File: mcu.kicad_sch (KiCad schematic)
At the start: 42 parts, among them J2 RJ45_Shielded, J4 Micro_SD_Card_Det1, J6 Conn_01x03_Pin, J7 RFShield_TwoPieces, SW1 SW_Push, SW2 SW_Push, SW3 SW_Push, SW4 SW_Push, U1 nRF54L15-QFXX, U9 TPD6F003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

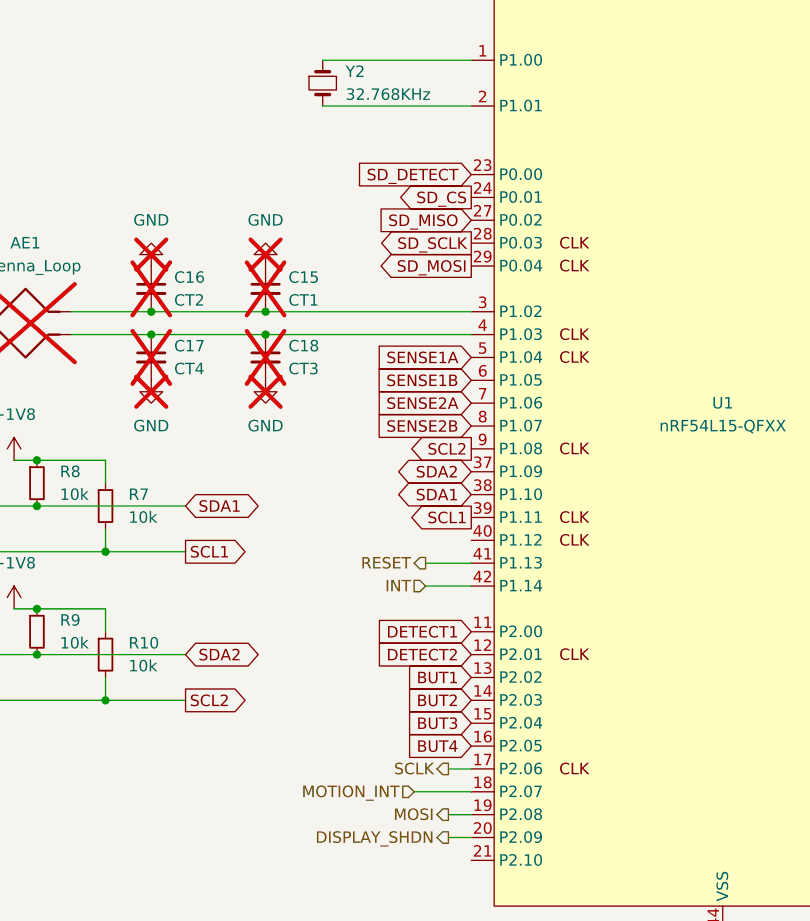
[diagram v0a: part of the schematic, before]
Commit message: start routing MCU + switch out pin assignments
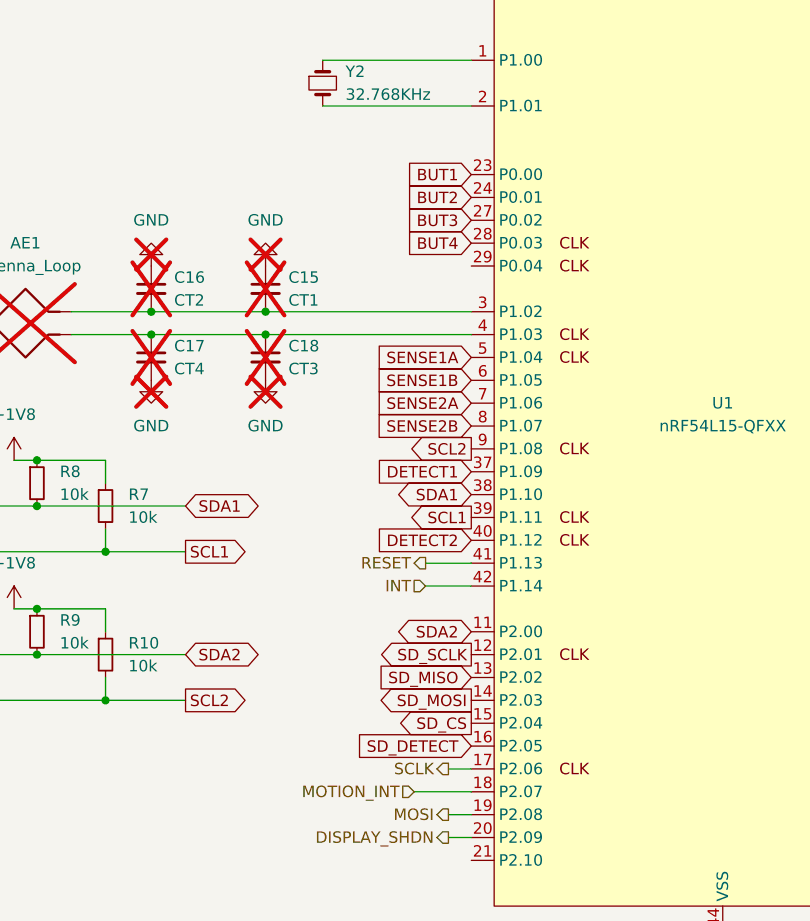
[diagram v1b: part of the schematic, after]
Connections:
- net BUT1: now also U1.23 (P0.00); no longer U1.13 (P2.02)
- net BUT2: now also U1.24 (P0.01); no longer U1.14 (P2.03)
- net BUT3: now also U1.27 (P0.02); no longer U1.15 (P2.04)
- net BUT4: now also U1.28 (P0.03); no longer U1.16 (P2.05)
- net DETECT1: now also U1.37 (P1.09); no longer U1.11 (P2.00)
- net DETECT2: now also U1.40 (P1.12); no longer U1.12 (P2.01)
- net SDA2: now also U1.11 (P2.00); no longer U1.37 (P1.09)
- net SD_CS: now also U1.15 (P2.04); no longer U1.24 (P0.01)
- net SD_DETECT: now also U1.16 (P2.05); no longer U1.23 (P0.00)
- net SD_MISO: now also U1.13 (P2.02); no longer U1.27 (P0.02)
- net SD_MOSI: now also U1.14 (P2.03); no longer U1.29 (P0.04)
- net SD_SCLK: now also U1.12 (P2.01); no longer U1.28 (P0.03)

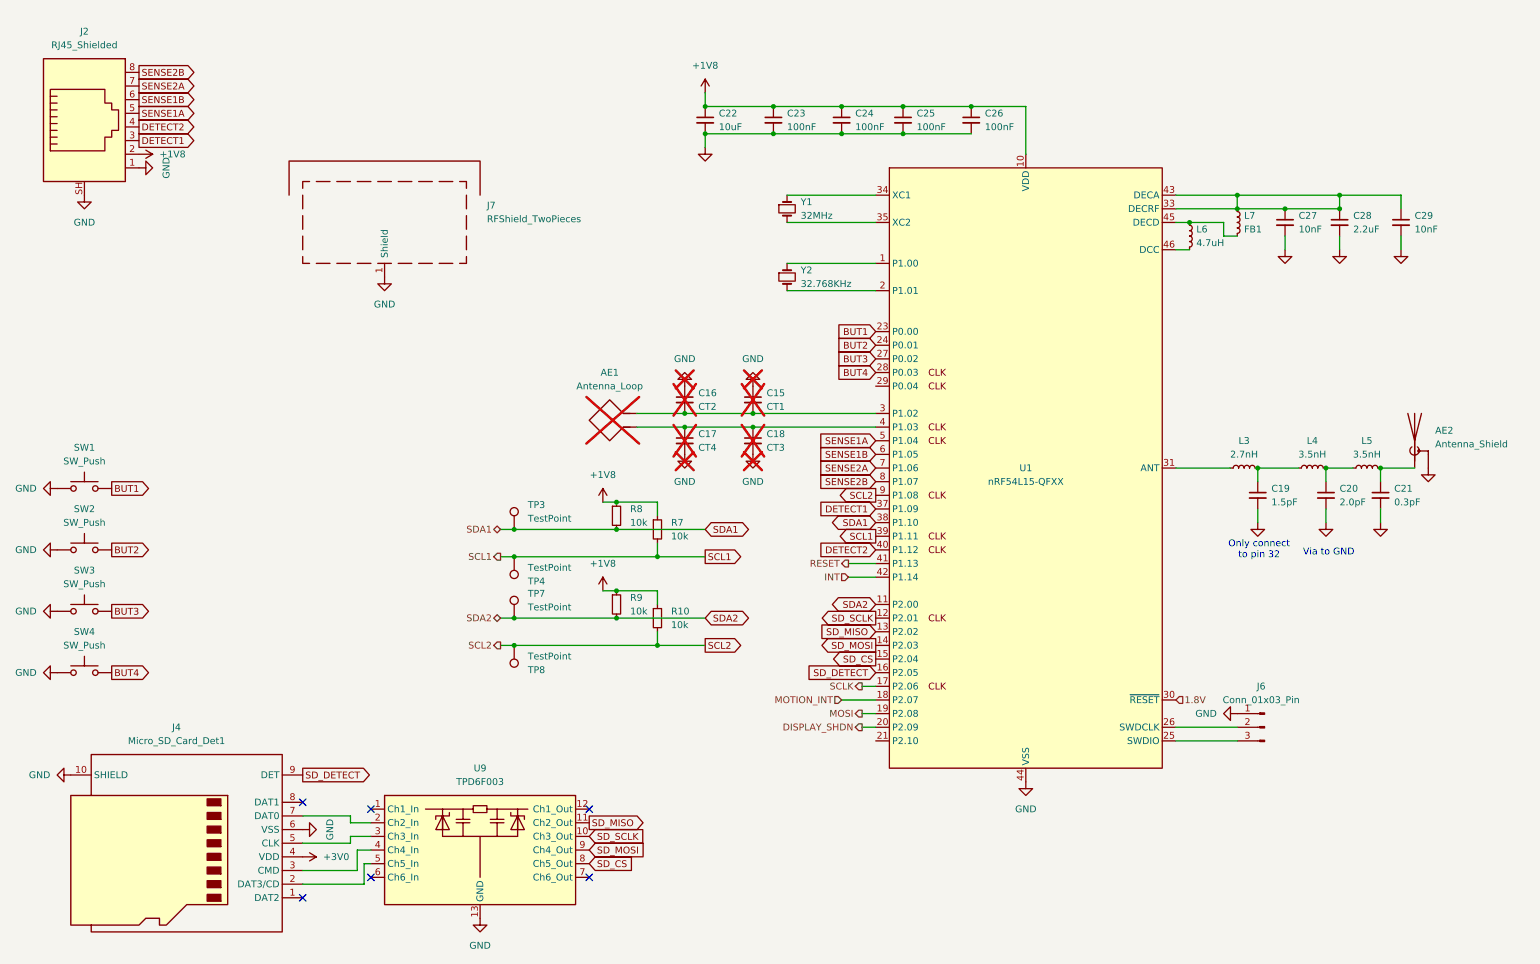
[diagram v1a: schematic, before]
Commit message: replace RJ45 with JST GH connector, add 2 I2C capable GPIOs to output port
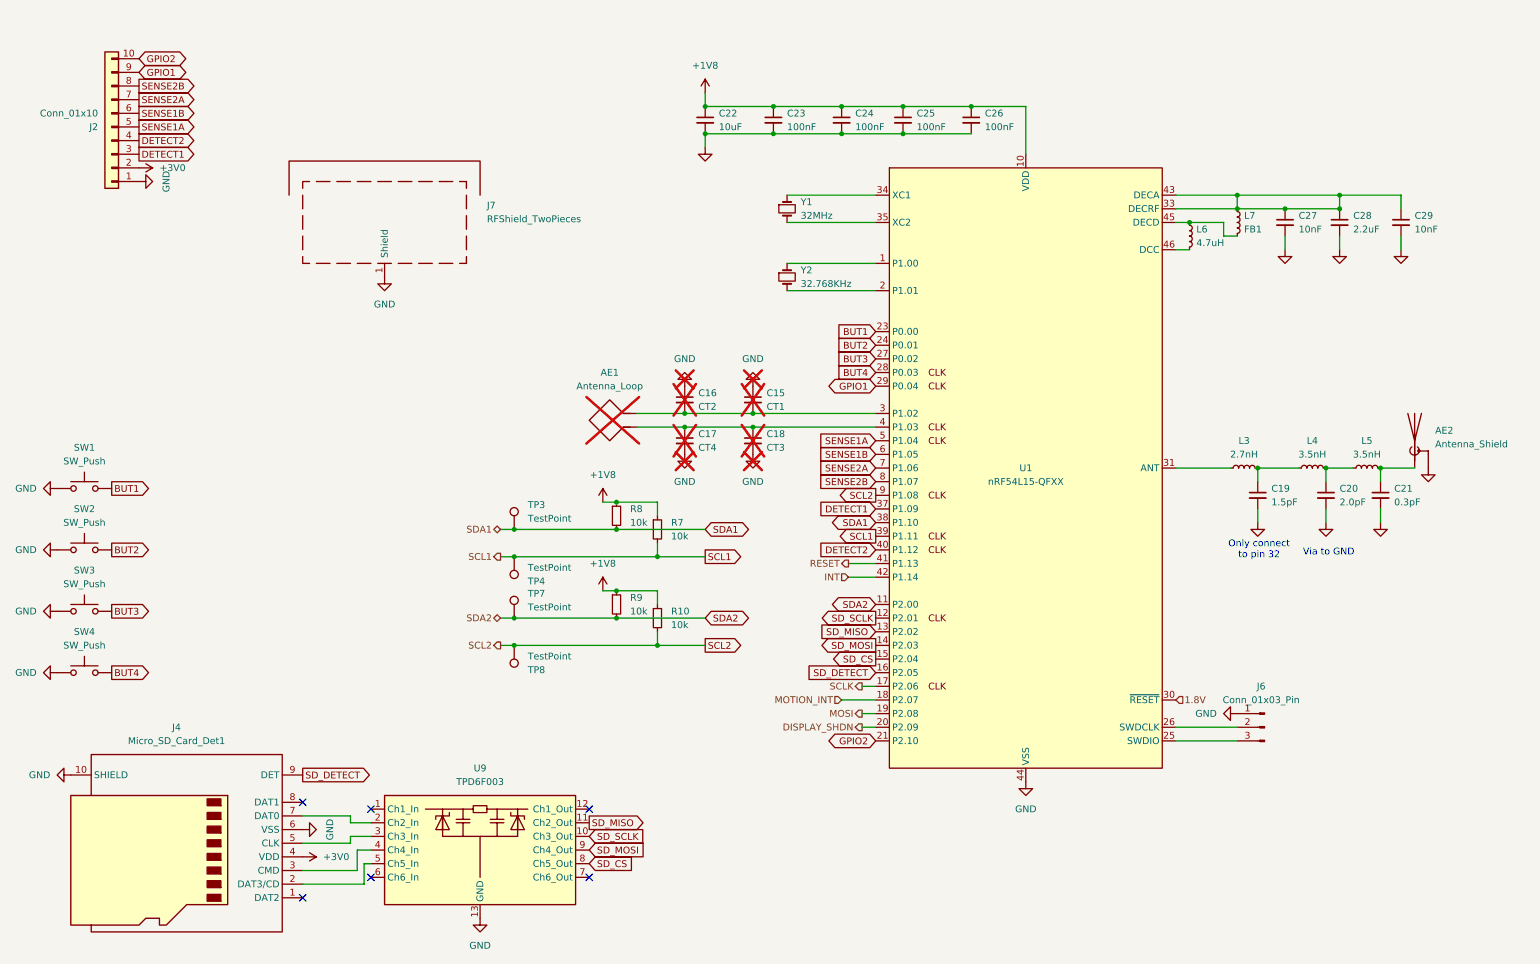
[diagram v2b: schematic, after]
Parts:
- removed J2: RJ45_Shielded, Connector_RJ:RJ45_Amphenol_RJHSE538X, symbol Connector:RJ45_Shielded
- added J2: Conn_01x10, Connector_JST:JST_GH_SM10B-GHS-TB_1x10-1MP_P1.25mm_Horizontal, symbol Connector_Generic:Conn_01x10
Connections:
- net +3V0: now also J2.2 (Pin_2)
- net DETECT1: now also J2.3 (Pin_3)
- net DETECT2: now also J2.4 (Pin_4)
- net GND: now also J2.1 (Pin_1)
- net SENSE1A: now also J2.5 (Pin_5)
- net SENSE1B: now also J2.6 (Pin_6)
- net SENSE2A: now also J2.7 (Pin_7)
- net SENSE2B: now also J2.8 (Pin_8)
- net GPIO2: now reaches U1.21 (P2.10)
- net GPIO2: now also J2.10 (Pin_10)
- net GPIO1: now reaches U1.29 (P0.04)
- net GPIO1: now also J2.9 (Pin_9)

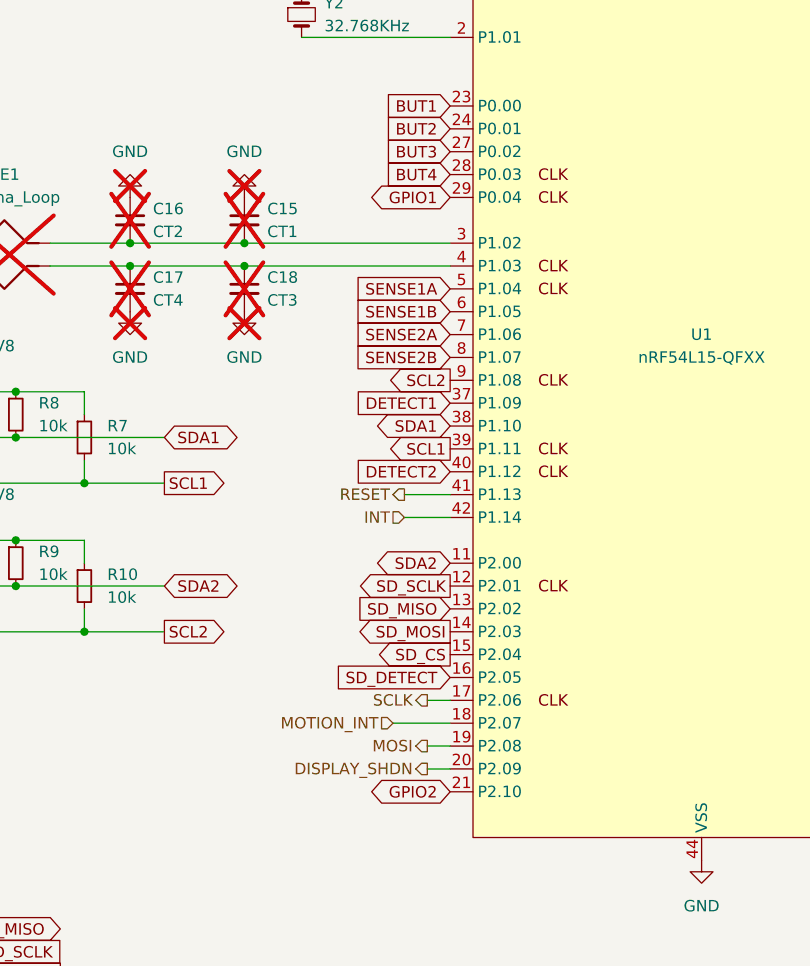
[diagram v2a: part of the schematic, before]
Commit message: rearrange output GPIO pin assignments to allow for more better things
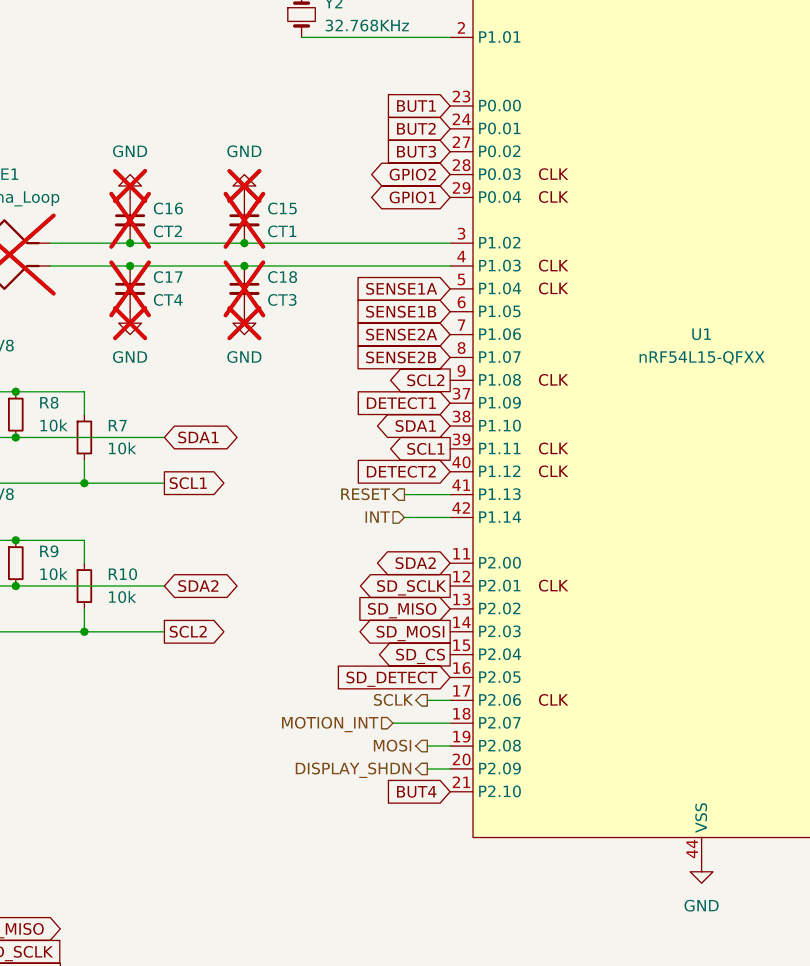
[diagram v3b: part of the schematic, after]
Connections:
- net BUT4: now also U1.21 (P2.10); no longer U1.28 (P0.03)
- net GPIO2: now also U1.28 (P0.03); no longer U1.21 (P2.10)
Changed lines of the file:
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@@
-		)
-	)
-	(global_label "SD_MOSI"
-		(shape input)
-		(at 123.19 171.45 0)
-		(fields_autoplaced yes)
-		(effects
-			(font
-				(size 1.27 1.27)
-			)
-			(justify left)
-		)
-		(property "Intersheetrefs" "${INTERSHEET_REFS}"
-			(at 134.2185 171.45 0)
-			(effects
-				(font
-					(size 1.27 1.27)
-				)
-				(justify left)
-				(hide yes)
-			)
-		)
-	)
-	(global_label "BUT2"
-		(shape output)
-		(at 34.29 115.57 0)
-		(fields_autoplaced yes)
-		(effects
-			(font
-				(size 1.27 1.27)
-			)
-			(justify left)
-		)
-		(property "Intersheetrefs" "${INTERSHEET_REFS}"
-			(at 42.0528 115.57 0)
-			(effects
-				(font
-					(size 1.27 1.27)
-				)
-				(justify left)
-				(hide yes)
-			)
-		)
-	)
-	(global_label "SENSE2B"
-		(shape output)
-		(at 39.37 29.21 0)
-		(fields_autoplaced yes)
-		(effects
-			(font
-				(size 1.27 1.27)
-			)
-			(justify left)
-		)
-		(property "Intersheetrefs" "${INTERSHEET_REFS}"
-			(at 50.8822 29.21 0)
-			(effects
-				(font
-					(size 1.27 1.27)
-				)
-				(justify left)
-				(hide yes)
-			)
-		)
-	)
-	(global_label "SENSE2A"
-		(shape output)
-		(at 39.37 31.75 0)
-		(fields_autoplaced yes)
-		(effects
-			(font
-				(size 1.27 1.27)
-			)
-			(justify left)
-		)
-		(property "Intersheetrefs" "${INTERSHEET_REFS}"
-			(at 50.7008 31.75 0)
-			(effects
-				(font
-					(size 1.27 1.27)
-				)
-				(justify left)
-				(hide yes)
-			)
 		)
 	)
 	(global_label "GPIO2"
 		(shape bidirectional)
-		(at 176.53 151.13 180)
-		(fields_autoplaced yes)
-		(effects
-			(font
-				(size 1.27 1.27)
-			)
-			(justify right)
-		)
-		(property "Intersheetrefs" "${INTERSHEET_REFS}"
-			(at 166.7487 151.13 0)
-			(effects
-				(font
-					(size 1.27 1.27)
-				)
-				(justify right)
+		(at 176.53 82.55 180)
+		(fields_autoplaced yes)
+		(effects
+			(font
+				(size 1.27 1.27)
+			)
+			(justify right)
+		)
+		(property "Intersheetrefs" "${INTERSHEET_REFS}"
+			(at 166.7487 82.55 0)
+			(effects
+				(font
+					(size 1.27 1.27)
+				)
+				(justify right)
+				(hide yes)
+			)
+		)
+	)
+	(global_label "SD_MOSI"
+		(shape input)
+		(at 123.19 171.45 0)
+		(fields_autoplaced yes)
+		(effects
+			(font
+				(size 1.27 1.27)
+			)
+			(justify left)
+		)
+		(property "Intersheetrefs" "${INTERSHEET_REFS}"
+			(at 134.2185 171.45 0)
+			(effects
+				(font
+					(size 1.27 1.27)
+				)
+				(justify left)
+				(hide yes)
+			)
+		)
+	)
+	(global_label "BUT2"
+		(shape output)
+		(at 34.29 115.57 0)
+		(fields_autoplaced yes)
+		(effects
+			(font
+				(size 1.27 1.27)
+			)
+			(justify left)
+		)
+		(property "Intersheetrefs" "${INTERSHEET_REFS}"
+			(at 42.0528 115.57 0)
+			(effects
+				(font
+					(size 1.27 1.27)
+				)
+				(justify left)
+				(hide yes)
+			)
+		)
+	)
+	(global_label "SENSE2B"
+		(shape output)
+		(at 39.37 29.21 0)
+		(fields_autoplaced yes)
+		(effects
+			(font
+				(size 1.27 1.27)
+			)
+			(justify left)
+		)
+		(property "Intersheetrefs" "${INTERSHEET_REFS}"
+			(at 50.8822 29.21 0)
+			(effects
+				(font
+					(size 1.27 1.27)
+				)
+				(justify left)
+				(hide yes)
+			)
+		)
+	)
+	(global_label "SENSE2A"
+		(shape output)
+		(at 39.37 31.75 0)
+		(fields_autoplaced yes)
+		(effects
+			(font
+				(size 1.27 1.27)
+			)
+			(justify left)
+		)
+		(property "Intersheetrefs" "${INTERSHEET_REFS}"
+			(at 50.7008 31.75 0)
+			(effects
+				(font
+					(size 1.27 1.27)
+				)
+				(justify left)
 				(hide yes)
 			)
@@
 		)
 	)
-	(global_label "BUT4"
-		(shape input)
-		(at 176.53 82.55 180)
-		(fields_autoplaced yes)
-		(effects
-			(font
-				(size 1.27 1.27)
-			)
-			(justify right)
-		)
-		(property "Intersheetrefs" "${INTERSHEET_REFS}"
-			(at 168.7672 82.55 0)
-			(effects
-				(font
-					(size 1.27 1.27)
-				)
-				(justify right)
-				(hide yes)
-			)
-		)
-	)
 	(global_label "SENSE1B"
 		(shape input)
@@
 				(hide yes)
 			)
+		)
+	)
+	(global_label "BUT4"
+		(shape input)
+		(at 176.53 151.13 180)
+		(fields_autoplaced yes)
+		(effects
+			(font
+				(size 1.27 1.27)
+			)
+			(justify right)
+		)
+		(property "Intersheetrefs" "${INTERSHEET_REFS}"
+			(at 168.7672 151.13 0)
+			(effects
+				(font
+					(size 1.27 1.27)
+				)
+				(justify right)
+				(hide yes)
+			)
